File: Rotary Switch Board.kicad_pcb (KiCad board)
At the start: 2 copper layers, 35.5 x 35.5 mm, 12 parts, among them J6 D2, SW1 1P8T_ROTARY_SWITCH

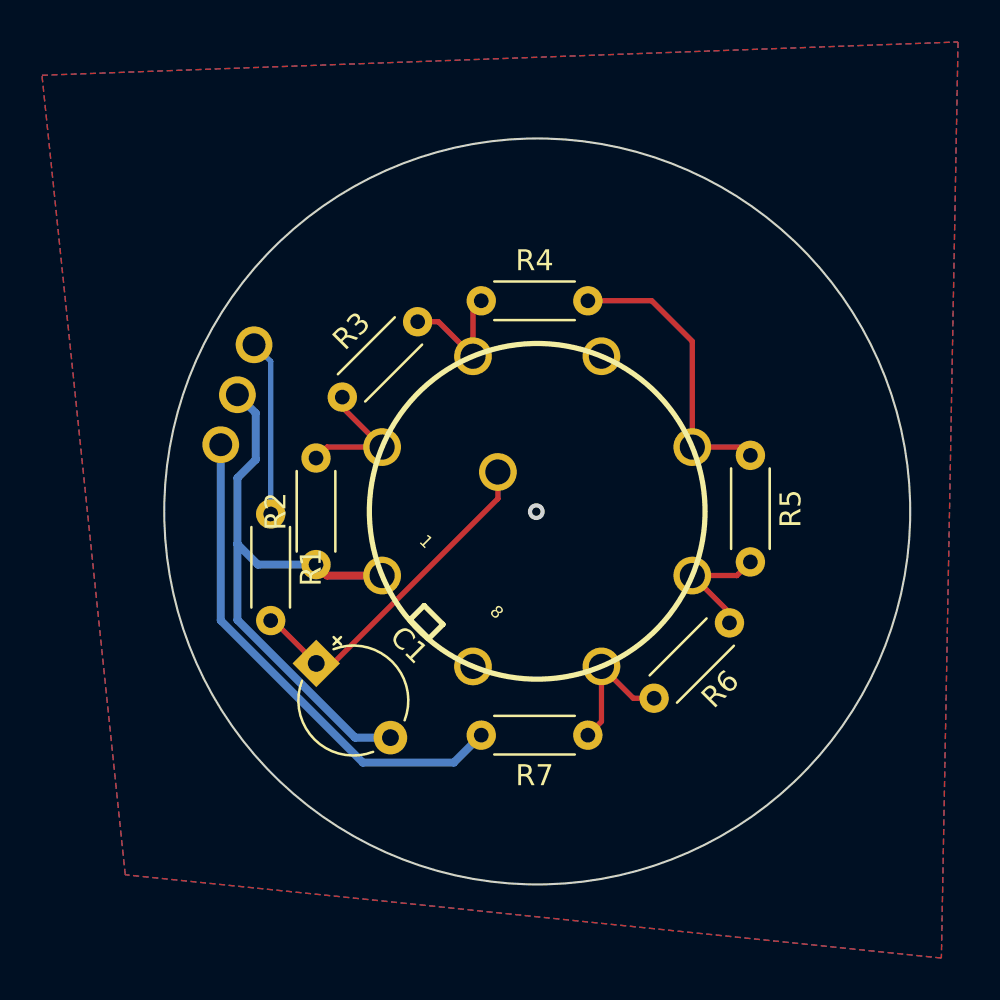
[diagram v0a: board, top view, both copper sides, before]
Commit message: included larger resistor
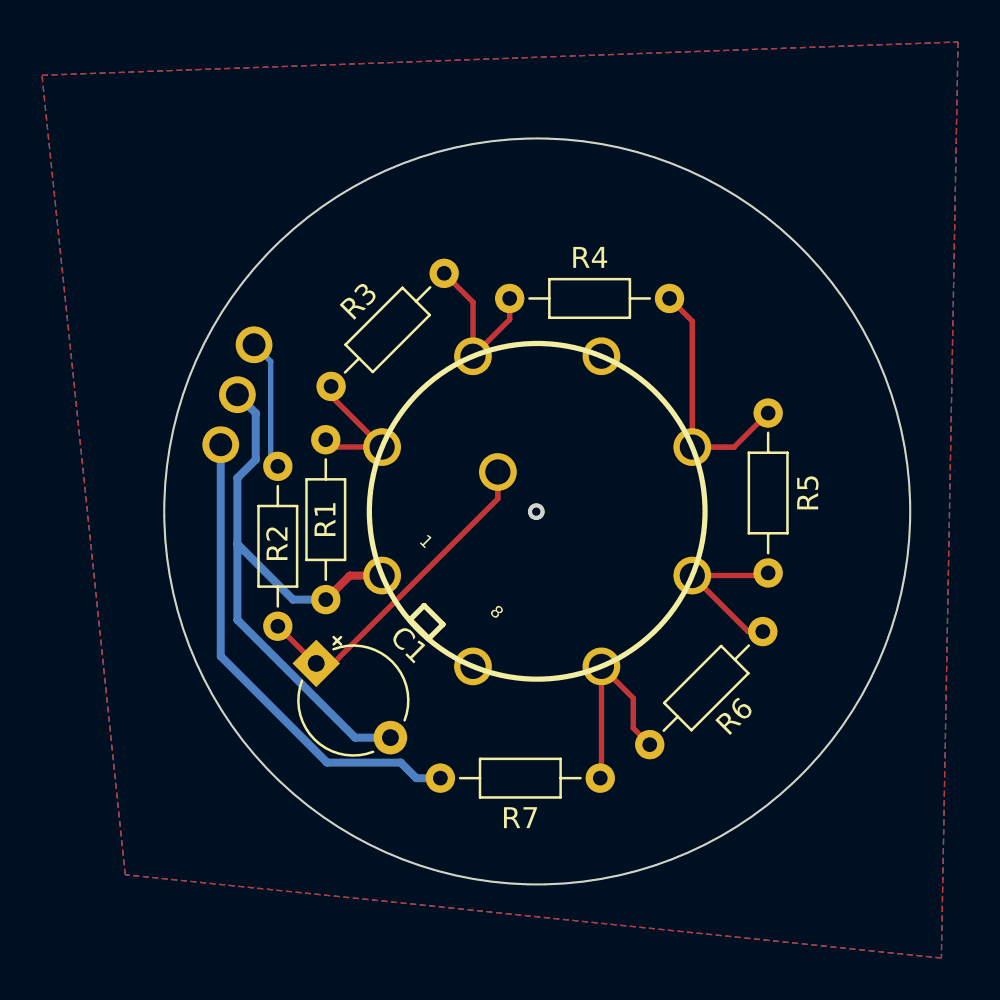
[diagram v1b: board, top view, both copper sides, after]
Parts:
- R1, R2, R3, R4, R5, R6, R7: footprint Resistor_THT:R_Axial_DIN0204_L3.6mm_D1.6mm_P5.08mm_Horizontal -> Resistor_THT:R_Axial_DIN0204_L3.6mm_D1.6mm_P7.62mm_Horizontal
- moved R1 2.29 mm to (127.1, 108.3)
- moved R5 2.19 mm to (150.5, 105.8)
- moved R7 2.13 mm to (142.5, 123.2)
- moved R2 1.73 mm to (129.4, 114.7)
- moved R6 1.64 mm to (150.2, 116.2)
- moved R4 1.36 mm to (138.2, 100.3)
- moved R3 0.74 mm to (129.7, 104.5)
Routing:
- net Net-(R6-Pad2): track 6.68 -> 10.0 mm
- net Signal: track 8.39 -> 6.26 mm
- net Net-(R5-Pad2): track 6.03 -> 8.13 mm
- net Net-(R4-Pad2): track 13.8 -> 11.8 mm
- net Net-(R3-Pad2): track 6.12 -> 8.00 mm
- net +5V: track 24.1 -> 23.0 mm
- net GND: track 28.6 -> 29.5 mm

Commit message: allowed for connection of all 8 pins, now you can just skip the ones you dont need
now you can just skip the ones you dont need
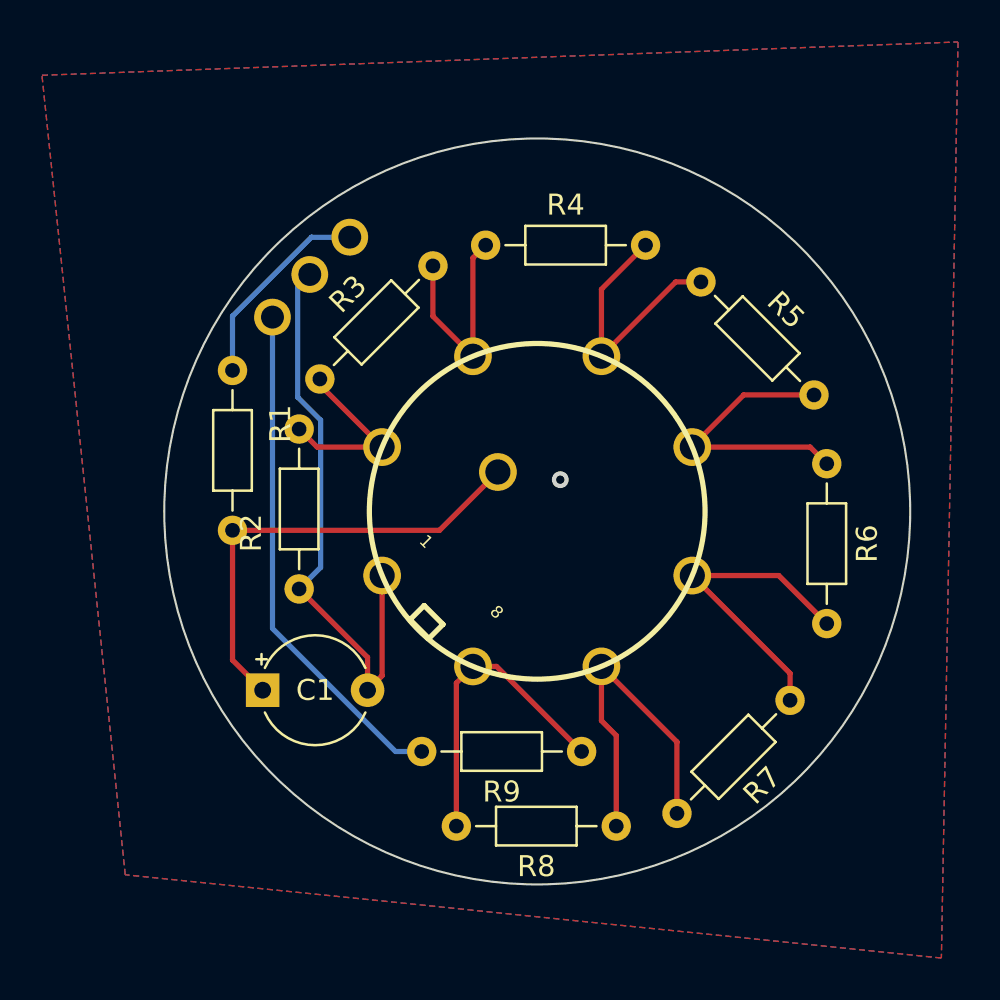
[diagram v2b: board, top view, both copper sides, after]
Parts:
- added R8: 1000Ω, Resistor_THT:R_Axial_DIN0204_L3.6mm_D1.6mm_P7.62mm_Horizontal, F.Cu at (143.3, 125.5)
- added R9: 1000Ω, Resistor_THT:R_Axial_DIN0204_L3.6mm_D1.6mm_P7.62mm_Horizontal, F.Cu at (141.6, 121.9)
- R2, R3, R4, R5, R6, R7: value 2000Ω -> 1000Ω
- moved R7 9.78 mm to (151.5, 119.5), turned to -135 degrees
- moved R6 8.56 mm to (153.3, 108.2), turned to -90 degrees
- moved R5 7.02 mm to (147.3, 99.5), turned to -45 degrees
- moved ? 6.86 mm to (130.6, 97.4)
- moved J6 6.69 mm to (128.7, 99.2)
- moved ? 6.56 mm to (126.9, 101.2)
- moved R1 5.06 mm to (125.0, 103.8)
- moved C1 2.85 mm to (126.4, 119.0), turned to 0 degrees
- moved R4 2.79 mm to (137.0, 97.8)
- moved R2 1.37 mm to (128.1, 114.2)
- moved R3 0.64 mm to (129.1, 104.2)
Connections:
- R7 pad 2: +5V -> Net-(R7-Pad2)
- SW1 pad 4: unconnected-(SW1-Pad4) -> Net-(R4-Pad2)
- SW1 pad 5: Net-(R4-Pad2) -> Net-(R5-Pad2)
- SW1 pad 6: Net-(R5-Pad2) -> Net-(R6-Pad2)
- SW1 pad 7: Net-(R6-Pad2) -> Net-(R7-Pad2)
- SW1 pad 8: unconnected-(SW1-Pad8) -> Net-(R8-Pad2)
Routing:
- net Net-(R7-Pad2): track 0.00 -> 16.4 mm
- net Net-(R8-Pad2): track 0.00 -> 14.8 mm
- net Net-(C1-Pad1): track 15.7 -> 22.0 mm
- net Net-(R5-Pad2): track 8.13 -> 13.6 mm
- net Net-(R6-Pad2): track 10.0 -> 15.2 mm
- net Signal: track 6.26 -> 9.73 mm
- net Net-(R3-Pad2): track 8.00 -> 10.6 mm
- net GND: track 29.5 -> 28.0 mm
- net +5V: track 23.0 -> 24.4 mm
- net Net-(R2-Pad2): track 8.01 -> 8.78 mm
- net Net-(R4-Pad2): track 11.8 -> 12.4 mm

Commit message: redid traces
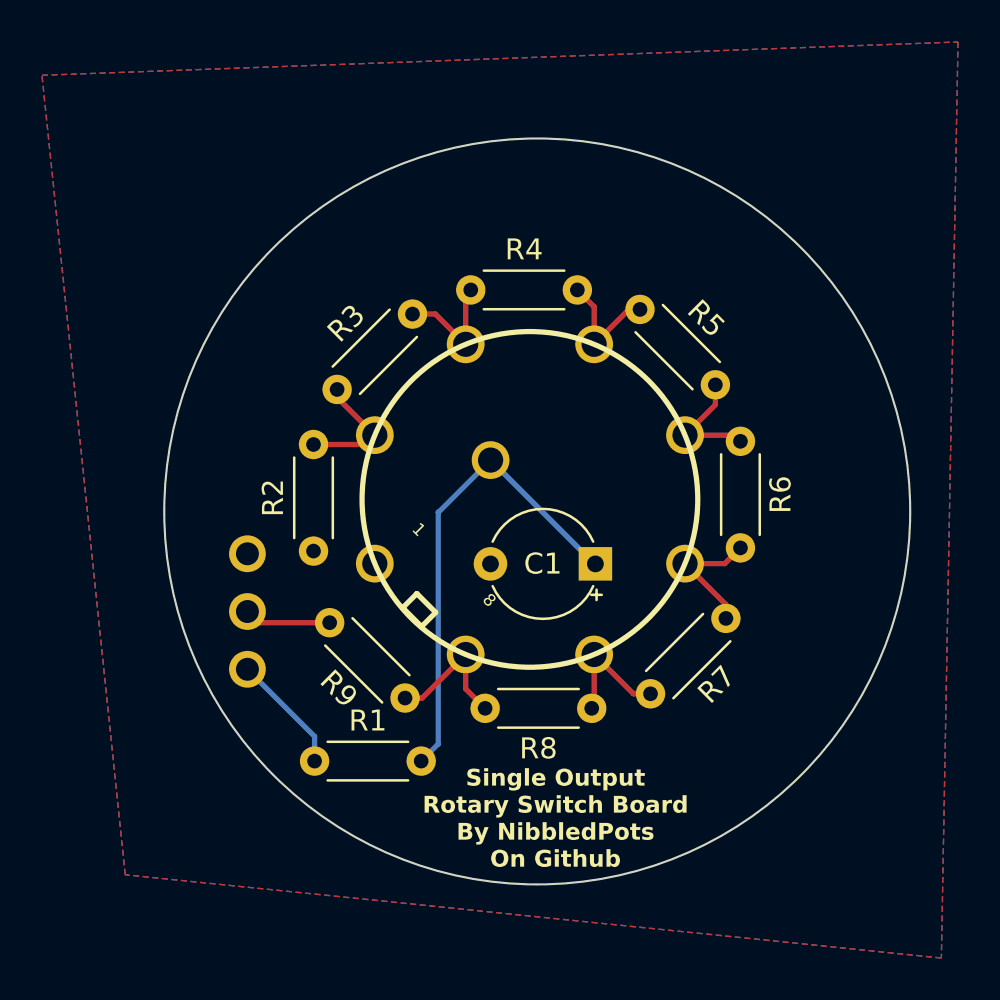
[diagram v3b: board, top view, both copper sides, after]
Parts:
- R1, R2, R3, R4, R5, R6, R7, R8, R9: footprint Resistor_THT:R_Axial_DIN0204_L3.6mm_D1.6mm_P7.62mm_Horizontal -> Resistor_THT:R_Axial_DIN0204_L3.6mm_D1.6mm_P5.08mm_Horizontal
- moved ? 21.2 mm to (125.7, 118.0), turned to 180 degrees
- moved R1 19.0 mm to (128.9, 122.4), turned to 0 degrees
- moved C1 17.0 mm to (142.3, 113.0), turned to 180 degrees
- moved ? 14.1 mm to (125.7, 115.2), turned to 180 degrees
- moved J6 13.6 mm to (125.7, 112.5), turned to 180 degrees
- moved R9 8.79 mm to (133.2, 119.4), turned to 135 degrees
- moved R8 5.73 mm to (142.1, 119.9)
- moved R7 4.96 mm to (148.5, 115.6)
- moved R6 4.25 mm to (149.2, 107.1)
- moved R5 3.19 mm to (144.4, 100.9)
- moved R4 2.25 mm to (136.3, 99.9)
- moved R2 1.93 mm to (128.8, 112.4)
- moved R3 0.96 mm to (130.0, 104.7)
- moved SW1 0.67 mm to (139.1, 109.9)
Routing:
- net GND: track 28.0 -> 0.00 mm, vias 1 -> 0
- net +5V: track 24.4 -> 4.14 mm
- net Net-(R7-Pad2): track 16.4 -> 6.08 mm
- net Net-(R6-Pad2): track 15.2 -> 6.37 mm
- net Net-(R8-Pad2): track 14.8 -> 6.70 mm
- net Net-(R5-Pad2): track 13.6 -> 5.76 mm
- net Net-(R4-Pad2): track 12.4 -> 5.80 mm
- net Net-(R3-Pad2): track 10.6 -> 5.82 mm
- net Signal: track 9.73 -> 5.70 mm
- net Net-(R2-Pad2): track 8.78 -> 6.03 mm
- net Net-(C1-Pad1): track 22.0 -> 22.8 mm
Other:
- board text added: "Single Output Rotary Switch Board By NibbledPots On Github"
- board text removed: "By NibbledPots"
- board text removed: "Rotary Switch Board"
- board text removed: "Single Output"
- board text removed: "on Github"
